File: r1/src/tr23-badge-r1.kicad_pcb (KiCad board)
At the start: 4 copper layers, 111.2 x 142.3 mm, 249 parts, among them J1 532610271, J2 USB-C-12, J3 USB-A-10mm-flangeless, J4 AFC07-S40ECA-00, J5 PJ-320D, J6 2x03-socket-2.54-through-board, J7 TF-15x15, J8 DNP, Q1 MMBT3904-TP, Q2 MMBT3904-TP, Q3 MMBT3904-TP, Q4 DMG2305UX-13, Q5 DMG2305UX-13, Q6 AP2302B, SW1 REV_TACT, SW10 REV_TACT, SW11 REV_TACT, SW12 REV_TACT, SW13 REV_TACT, SW14 REV_TACT, SW15 REV_TACT, SW16 REV_TACT, SW17 REV_TACT, SW18 REV_TACT, SW19 REV_TACT, SW2 REV_TACT, SW20 REV_TACT, SW21 REV_TACT, SW22 REV_TACT, SW23 REV_TACT, SW24 REV_TACT, SW25 REV_TACT, SW26 REV_TACT, SW27 REV_TACT, SW28 REV_TACT, SW29 REV_TACT, SW3 REV_TACT, SW30 REV_TACT, SW31 REV_TACT, SW32 REV_TACT, SW33 REV_TACT, SW34 REV_TACT, SW4 REV_TACT, SW5 REV_TACT, SW6 REV_TACT, SW7 REV_TACT, SW8 REV_TACT, SW9 REV_TACT, U1 MCP73831T-2ACI_OT, U2 AP2114H-3_3TRG1, U3 CP2102N-A01-GQFN24, U4 PCM5100APW, U5 PAM8908, U6 PCA9555PW, U7 PCA9555PW, U8 PCA9555PW, U9 CC1200, Y1 32.768kHz, Y2 40Mhz

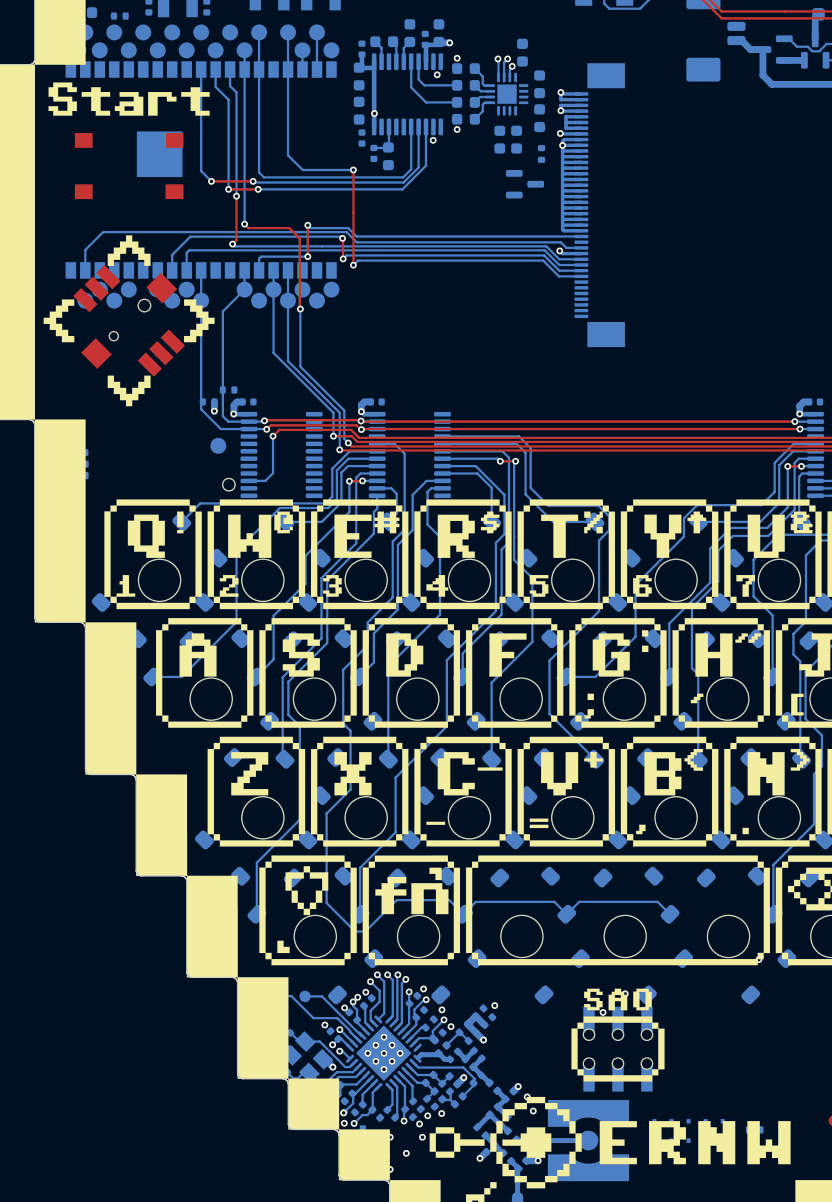
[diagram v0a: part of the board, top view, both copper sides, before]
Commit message: Radio routed
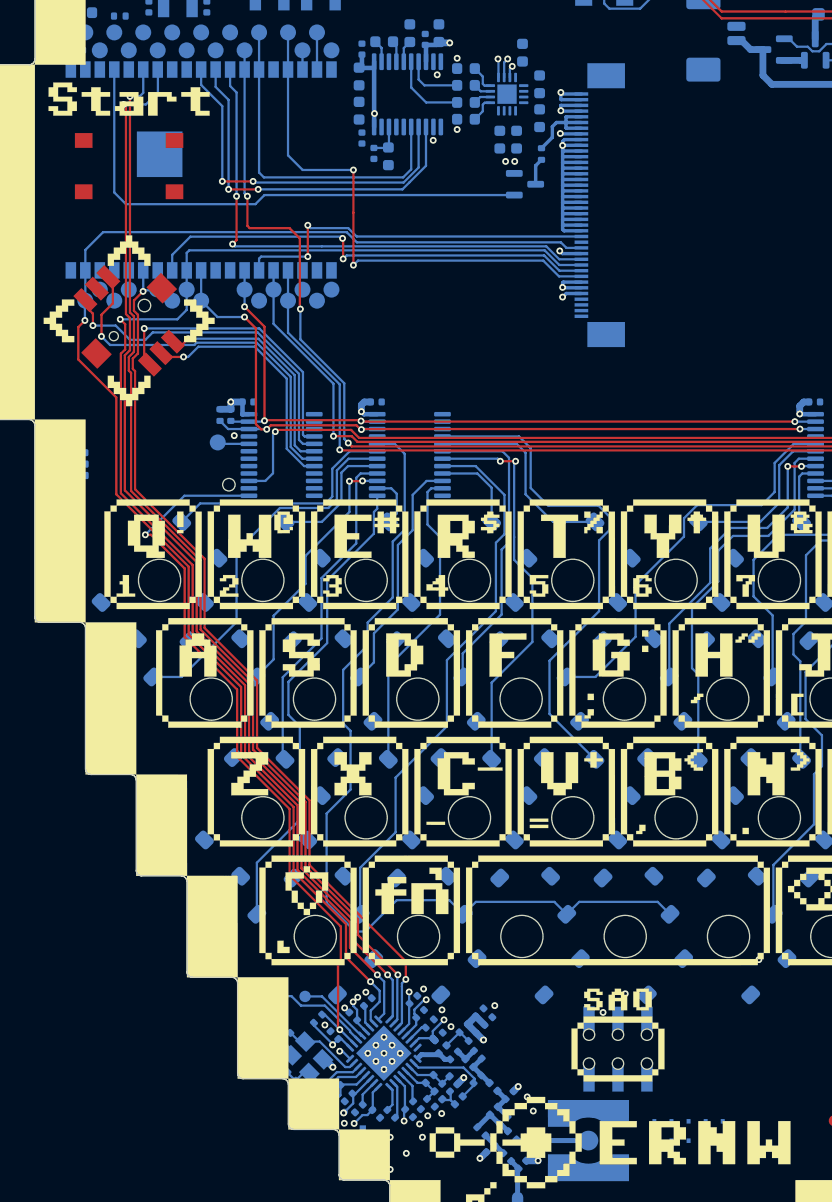
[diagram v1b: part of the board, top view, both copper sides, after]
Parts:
- moved R28 39.5 mm to (-26.3, -31.9), turned to 45 degrees
- moved R4 2.21 mm to (-34.0, -84.9), turned to -90 degrees
- moved R5 1.52 mm to (-34.9, -84.9), turned to -90 degrees
- moved TP33 0.30 mm to (-35.1, -82.5)
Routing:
- net /MISO: track 4.23 -> 96.0 mm, vias 1 -> 2
- net /CC_INT: track 4.43 -> 94.9 mm, vias 1 -> 2
- net /SCK: track 41.2 -> 118.0 mm, vias 1 -> 2
- net /~{CC_CS}: track 4.53 -> 78.6 mm, vias 1 -> 2
- net /MOSI: track 51.0 -> 124.2 mm, vias 1 -> 2
- net /CC_RESET: track 1.76 -> 65.3 mm, vias 2 -> 3
- net /BACKLIGHT: track 0.00 -> 46.6 mm
- net /io_expander/JOY_D: track 0.00 -> 32.7 mm, vias 0 -> 1
- net /io_expander/JOY_B: track 0.00 -> 30.2 mm, vias 0 -> 2
- net /io_expander/JOY_A: track 0.00 -> 25.4 mm, vias 0 -> 1
- net /io_expander/JOY_PUSH: track 0.00 -> 21.9 mm, vias 0 -> 1
- net /io_expander/JOY_C: track 0.00 -> 20.6 mm, vias 0 -> 1
- net +3.3V: track 87.7 -> 94.5 mm
- net /SCL: track 68.5 -> 72.3 mm, vias 4 -> 5
- net Net-(J4-Pin_34): track 5.03 -> 8.68 mm
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
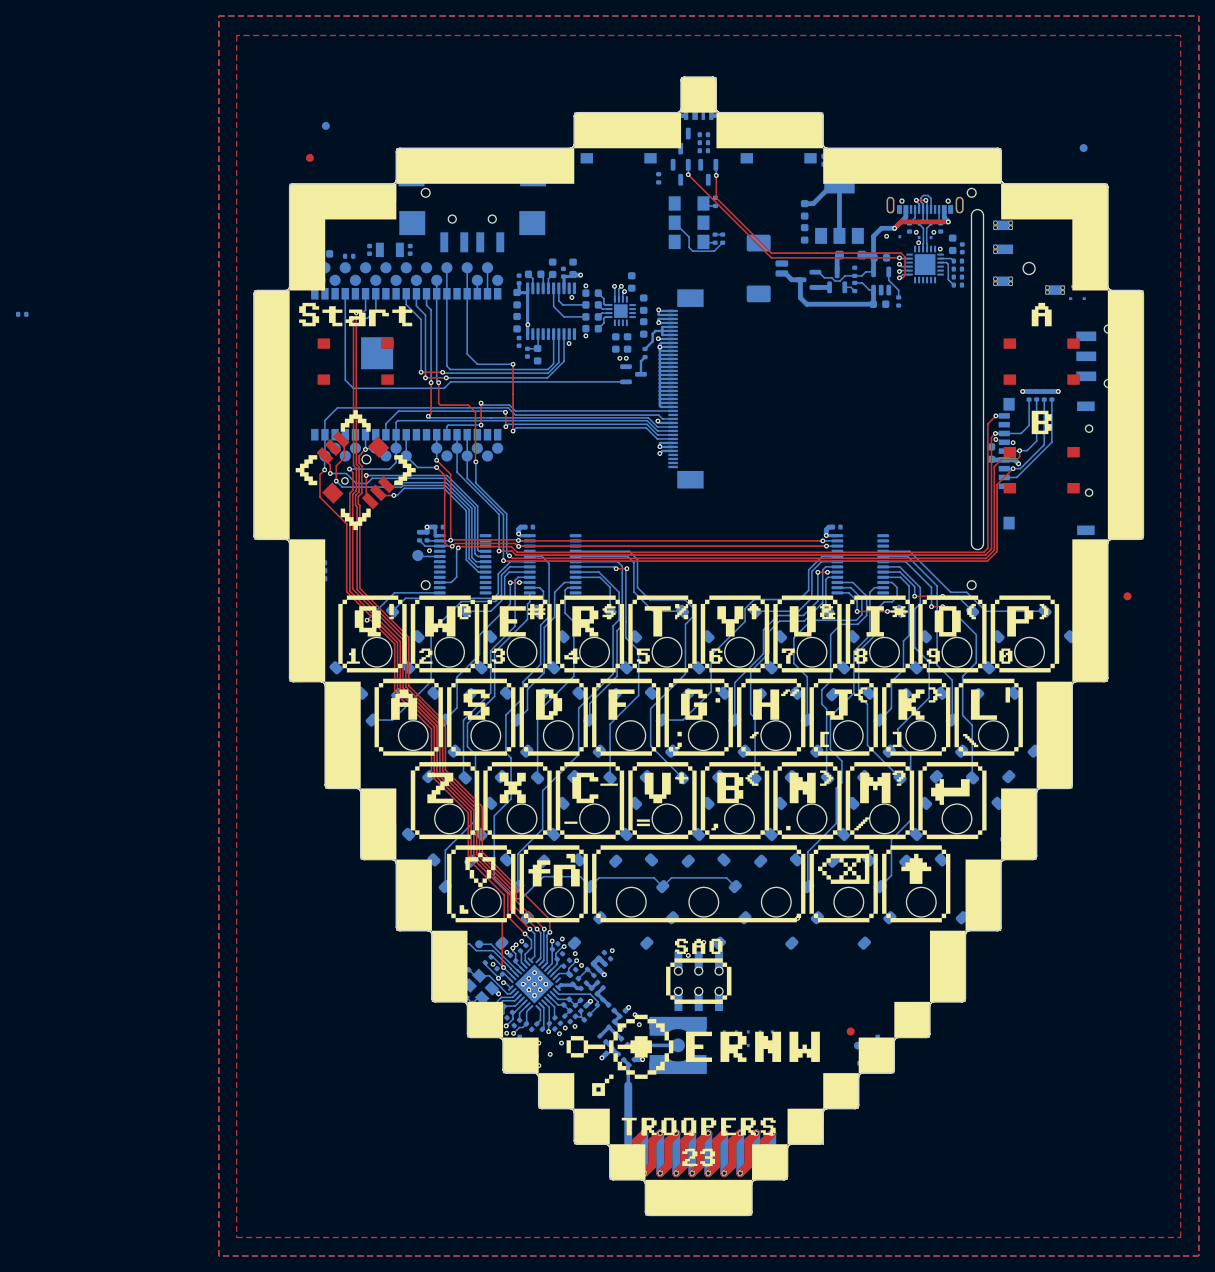
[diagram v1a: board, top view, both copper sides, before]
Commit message: Correct power switch footprint
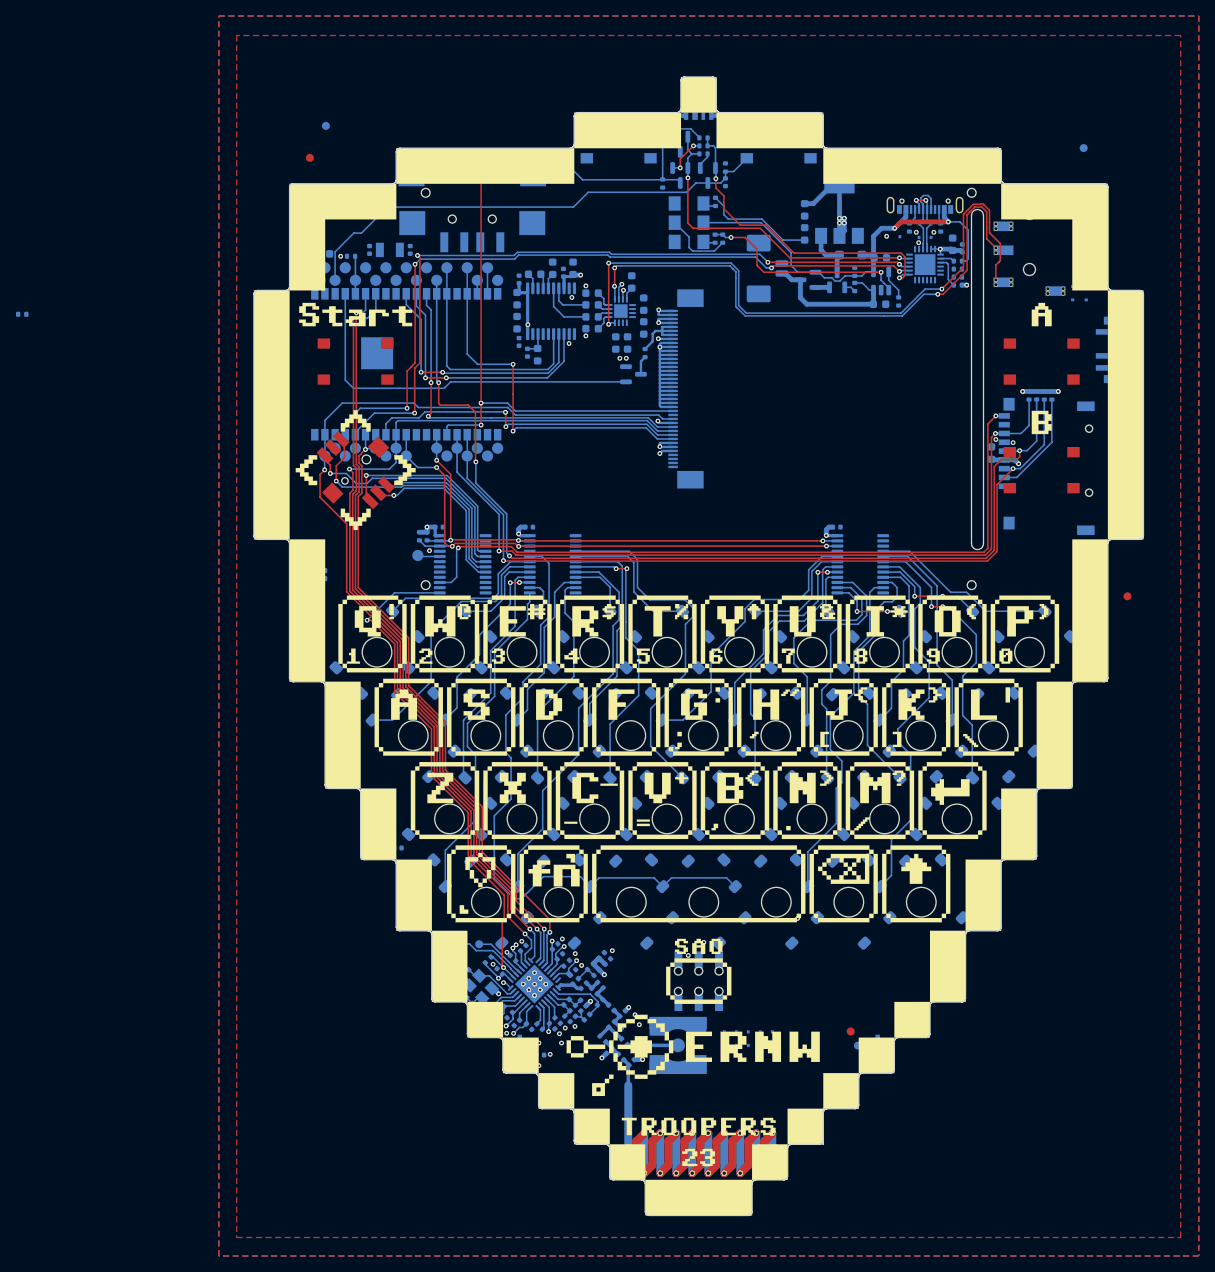
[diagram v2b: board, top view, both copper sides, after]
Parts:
- S3: footprint jeffmakes-footprints:SW_JS102011SAQN -> Button_Switch_SMD:SW_SPDT_PCM12
- moved C5 12.9 mm to (3.35, -129.2), turned to -90 degrees
- moved R7 12.8 mm to (3.35, -131.0), turned to -90 degrees
- moved S3 1.01 mm to (51.8, -108.2)
- moved C71 0.97 mm to (4.45, -137.3)
- moved C32 0.97 mm to (-37.6, -45.9)
- moved C36 0.97 mm to (48.8, -81.7)
- moved C70 0.97 mm to (50.2, -125.2)
- moved C34 0.97 mm to (21.5, -19.2)
- moved C33 0.97 mm to (-19.8, -20.1)
- moved C72 0.97 mm to (-47.5, -125.5)
- moved C35 0.97 mm to (39.4, -47.2)
- moved C31 0.91 mm to (-47.0, -82.5), turned to 90 degrees
- moved R6 0.82 mm to (-4.50, -129.0), turned to 90 degrees
- moved Q1 0.40 mm to (1.15, -130.0)
- moved Q2 0.40 mm to (-2.30, -130.0)
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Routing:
- net /TXD0: track 1.31 -> 91.8 mm, vias 1 -> 4
- net /RXD0: track 1.38 -> 91.2 mm, vias 1 -> 4
- net /audio/OUTL: track 0.00 -> 80.6 mm, vias 0 -> 3
- net /audio/OUTR: track 1.65 -> 70.6 mm, vias 1 -> 3
- net /~{RESET}: track 32.5 -> 96.9 mm, vias 2 -> 3
- net /EN: track 0.00 -> 60.4 mm
- net Net-(U1-STAT): track 0.95 -> 26.5 mm, vias 0 -> 2
- net VBUS: track 28.5 -> 53.4 mm
- net +VSW: track 2.27 -> 20.6 mm
- net /DTR: track 33.2 -> 41.7 mm
- net +3.3V: track 94.5 -> 102.9 mm, vias 25 -> 31
- net Net-(Q2-B): track 0.00 -> 5.13 mm, vias 0 -> 2
- net /KEY_INT: track 0.00 -> 4.70 mm
- net Net-(Q3-B): track 0.00 -> 4.52 mm
- net /RTS: track 35.4 -> 39.8 mm
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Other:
- board text added: "OFF"
- board text added: "ON"

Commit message: Speaker connector and mute switch
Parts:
- added J9: 532610271, Connector_Molex:Molex_PicoBlade_53261-0271_1x02-1MP_P1.25mm_Horizontal, B.Cu at (19.7, -29.1)
- added NT1: NetTie_2, NetTie:NetTie-2_SMD_Pad0.5mm, F.Cu at (-64.0, -75.6)
- added S8: K3-1296S-J1, Button_Switch_SMD:SW_SPDT_PCM12, B.Cu at (28.9, -30.2)
- moved FID3 17.3 mm to (30.4, -9.90)
- moved FID6 13.6 mm to (32.3, -15.6)
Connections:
- U5 pad 15: GND -> /audio/SGND
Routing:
- net /KEY_INT: track 4.70 -> 106.3 mm, vias 0 -> 6
- net /audio/SPK: track 0.00 -> 12.3 mm
- net /32K_XN: track 0.00 -> 7.38 mm
- net /32K_XP: track 0.00 -> 6.61 mm
- net GND: track 52.3 -> 54.1 mm
- net /EN: track 60.4 -> 62.1 mm
- net /I2S_SCK: vias 2 -> 0
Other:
- board text added: "Mute"

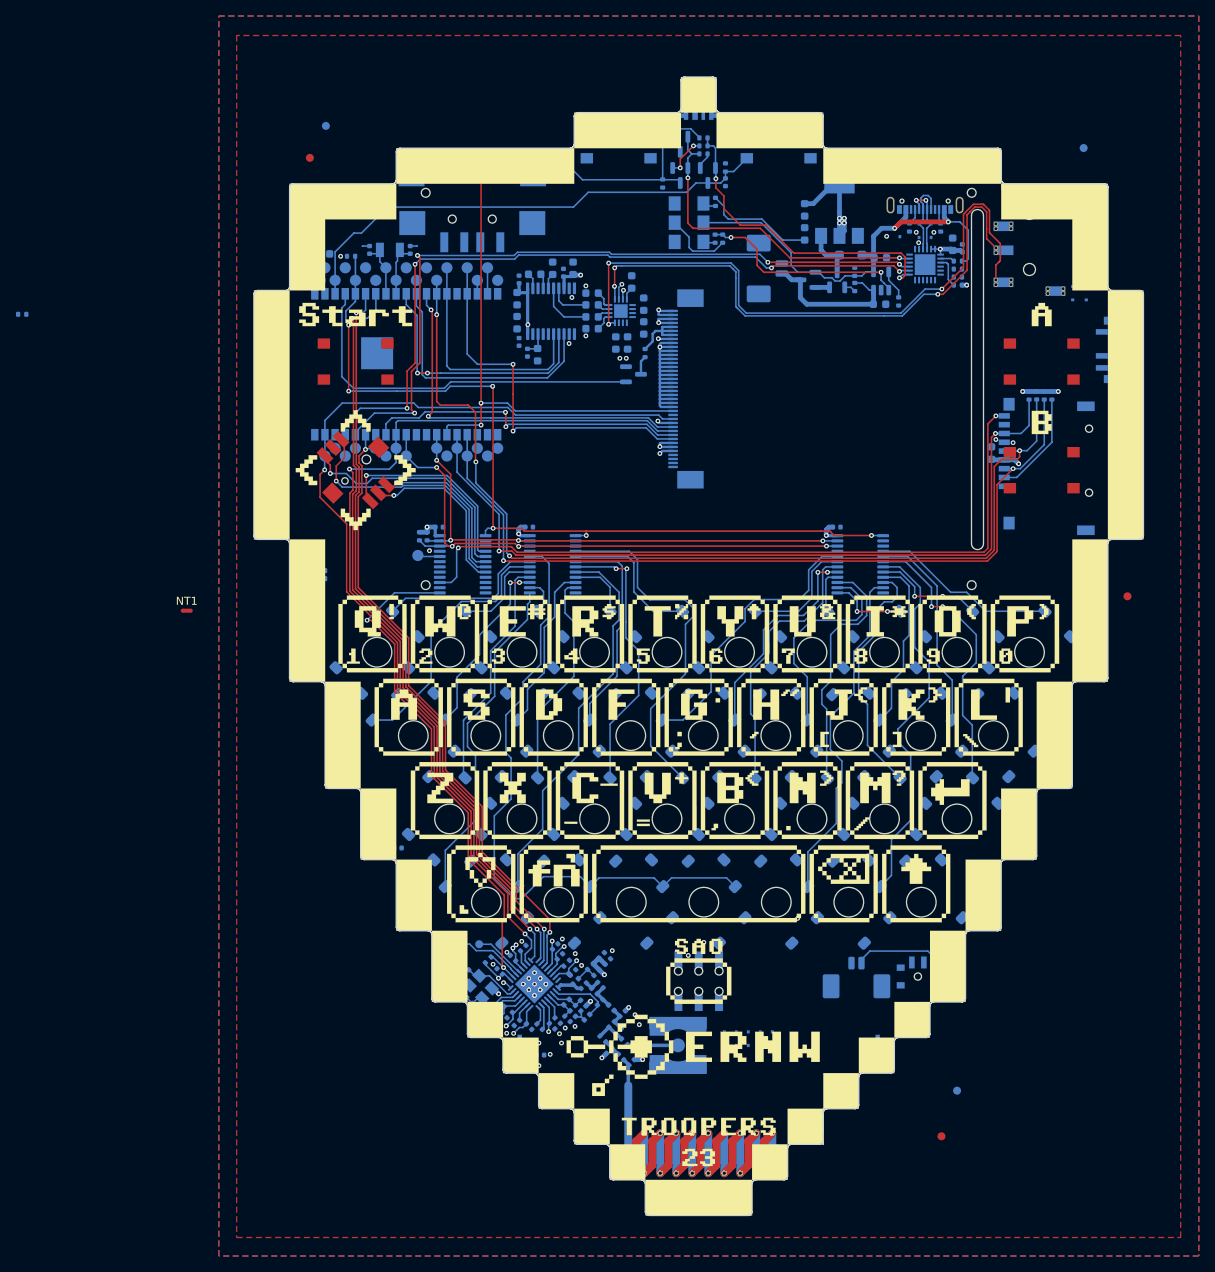
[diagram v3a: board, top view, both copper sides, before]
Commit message: Mute switch and speaker routing
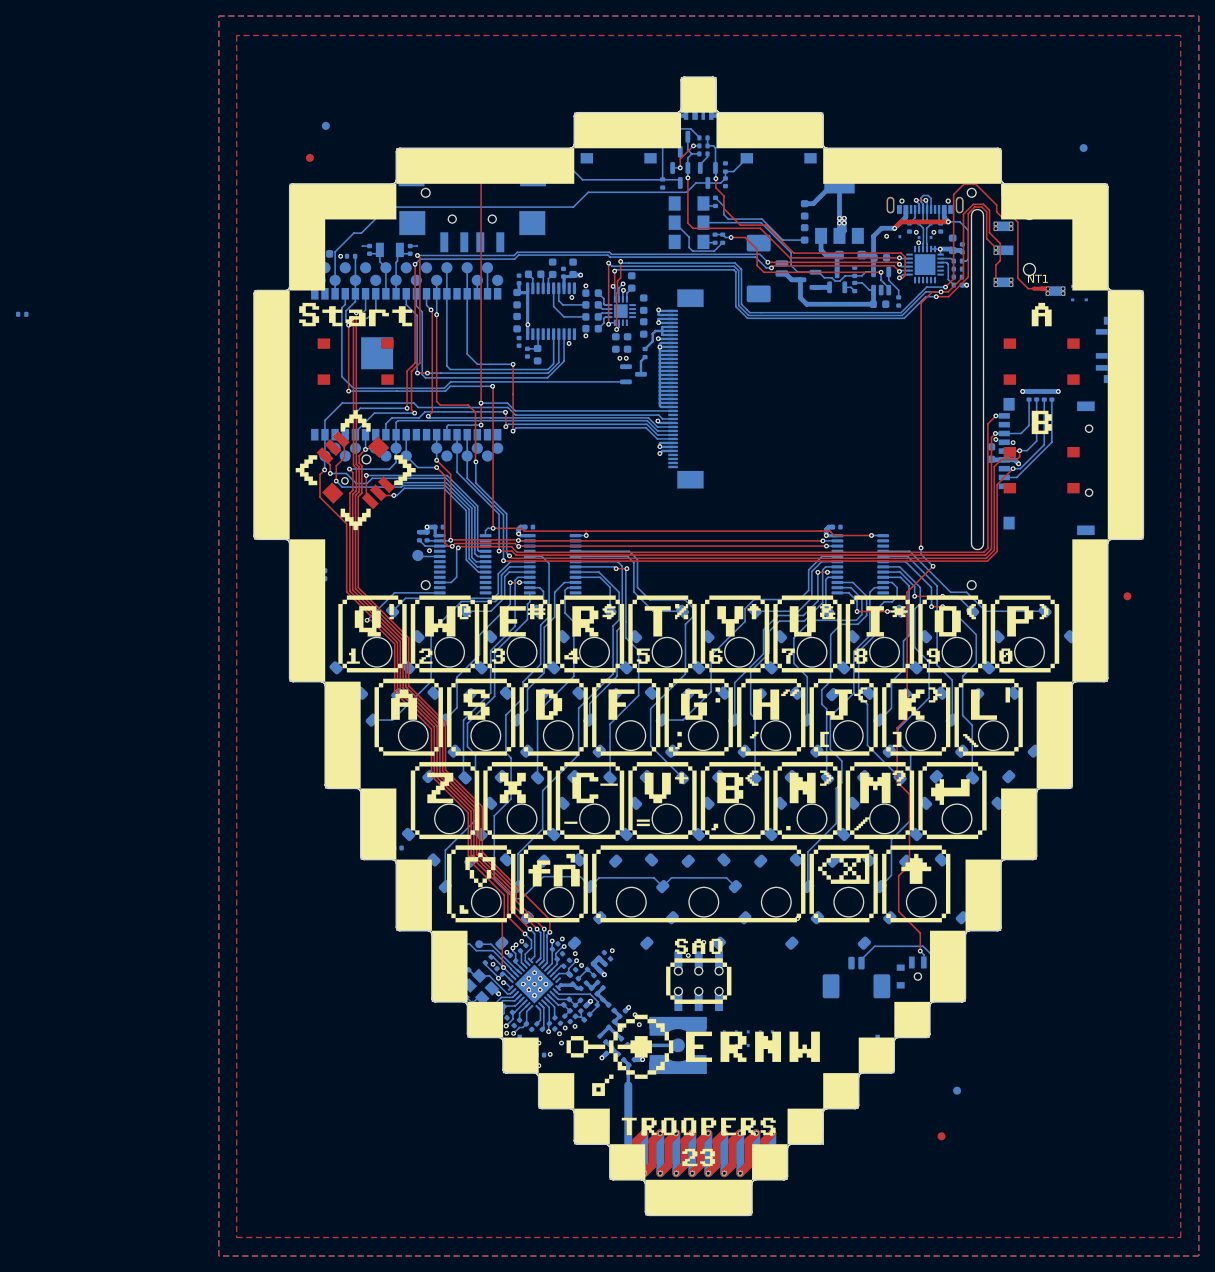
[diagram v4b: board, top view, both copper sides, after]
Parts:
- moved NT1 113.8 mm to (42.4, -115.8)
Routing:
- net /audio/OUTL: track 80.6 -> 172.0 mm, vias 3 -> 6
- net /audio/SGND: track 0.00 -> 89.3 mm, vias 0 -> 3
- net GND: track 54.1 -> 54.8 mm
